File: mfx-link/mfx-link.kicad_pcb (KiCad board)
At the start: 2 copper layers, 50 x 50 mm, 59 parts, among them P1 CONN_01X02, P2 CONN_02X03, P3 CONN_01X02, P4 Grove I2C, P5 IBT-2, P6 CONN_01X02, P7 CONN_01X03, P8 Grove UART, P9 MFX, Q1 BC547, Q2 BC547, Q3 BC547, SW1 SW_PUSH, U1 LM393-1, U2 7805, U3 PIC16F1705, U4 6N137, U5 7805

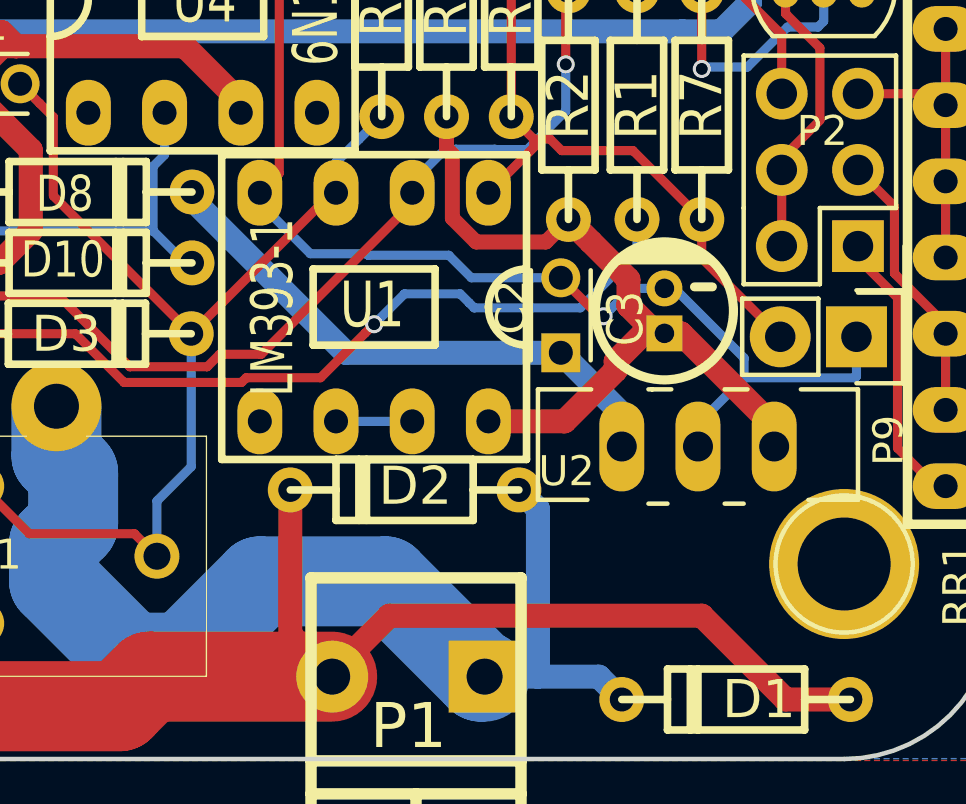
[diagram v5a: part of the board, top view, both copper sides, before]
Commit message: change caps
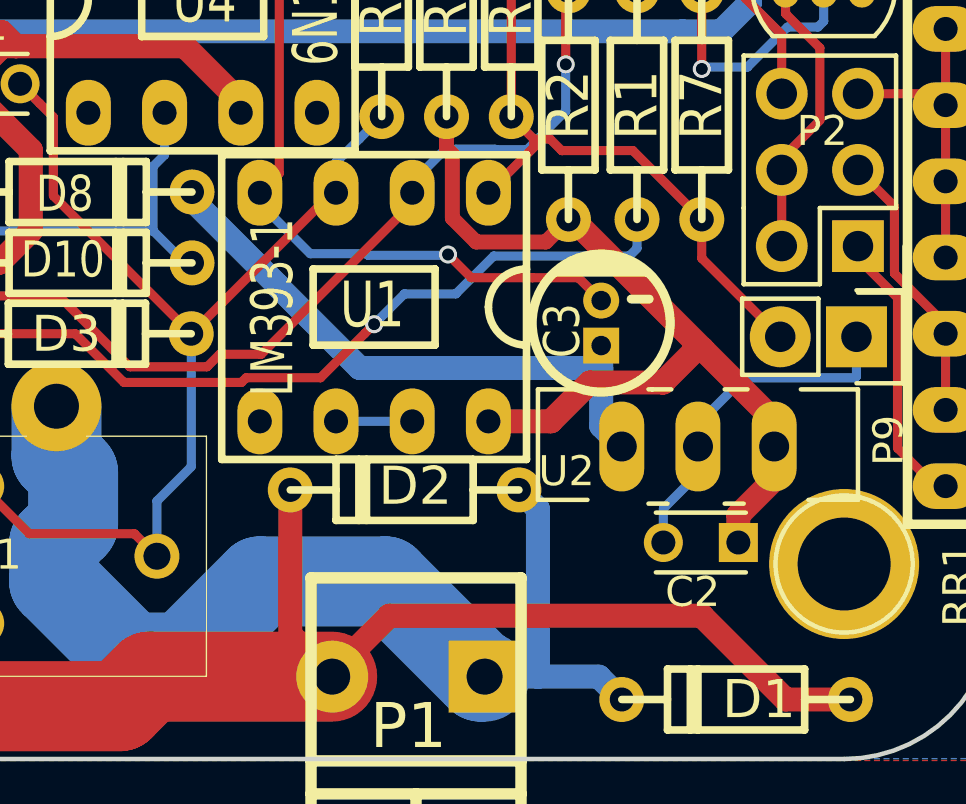
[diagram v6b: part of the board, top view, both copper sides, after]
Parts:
- Q1, Q2: value BC547 -> BC337
- moved C2 8.66 mm to (136.5, 122.8), turned to 180 degrees
- moved C3 2.15 mm to (131.9, 115.5)
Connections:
- C2 pad 1: /GVI -> VCC
- C3 pad 1: VCC -> /GVI
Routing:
- net VCC: track 26.1 -> 30.3 mm
- net GND: track 83.1 -> 79.9 mm
- net /GVI: track 18.8 -> 21.3 mm

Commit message: optimize placement
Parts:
- D8: value D -> 1N4007
- moved C2 3.90 mm to (132.6, 123.1), turned to 0 degrees
- moved C3 1.19 mm to (133.1, 115.4), turned to 90 degrees
- moved R14 0.38 mm to (112.1, 91.4)
- moved R12 0.25 mm to (109.9, 91.4)
- moved R10 0.13 mm to (107.6, 91.4)
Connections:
- C2 pad 1: VCC -> /GVI
- C3 pad 1: /GVI -> VCC
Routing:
- net GND: track 79.9 -> 102.9 mm, vias 8 -> 11
- net Net-(D11-Pad2): track 20.1 -> 16.8 mm, vias 2 -> 0
- net VCC: track 30.3 -> 27.6 mm
- net VDD: track 86.2 -> 87.7 mm
- net /GVI: track 21.3 -> 22.3 mm
- net Net-(P7-Pad2): track 23.8 -> 24.4 mm
- net /PULSE: track 48.4 -> 48.9 mm, vias 1 -> 2
- net GNDA: track 83.7 -> 83.5 mm, vias 6 -> 5

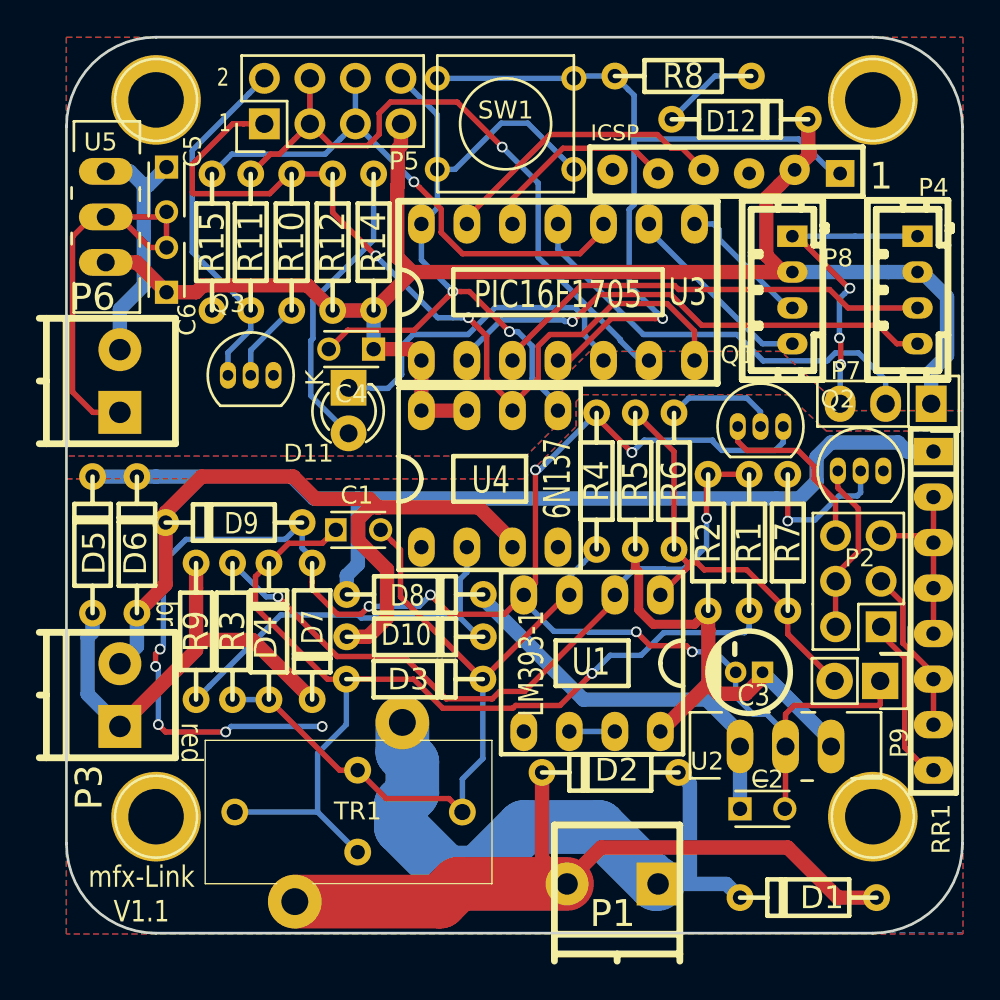
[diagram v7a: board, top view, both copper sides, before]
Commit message: fix BAT43 direction
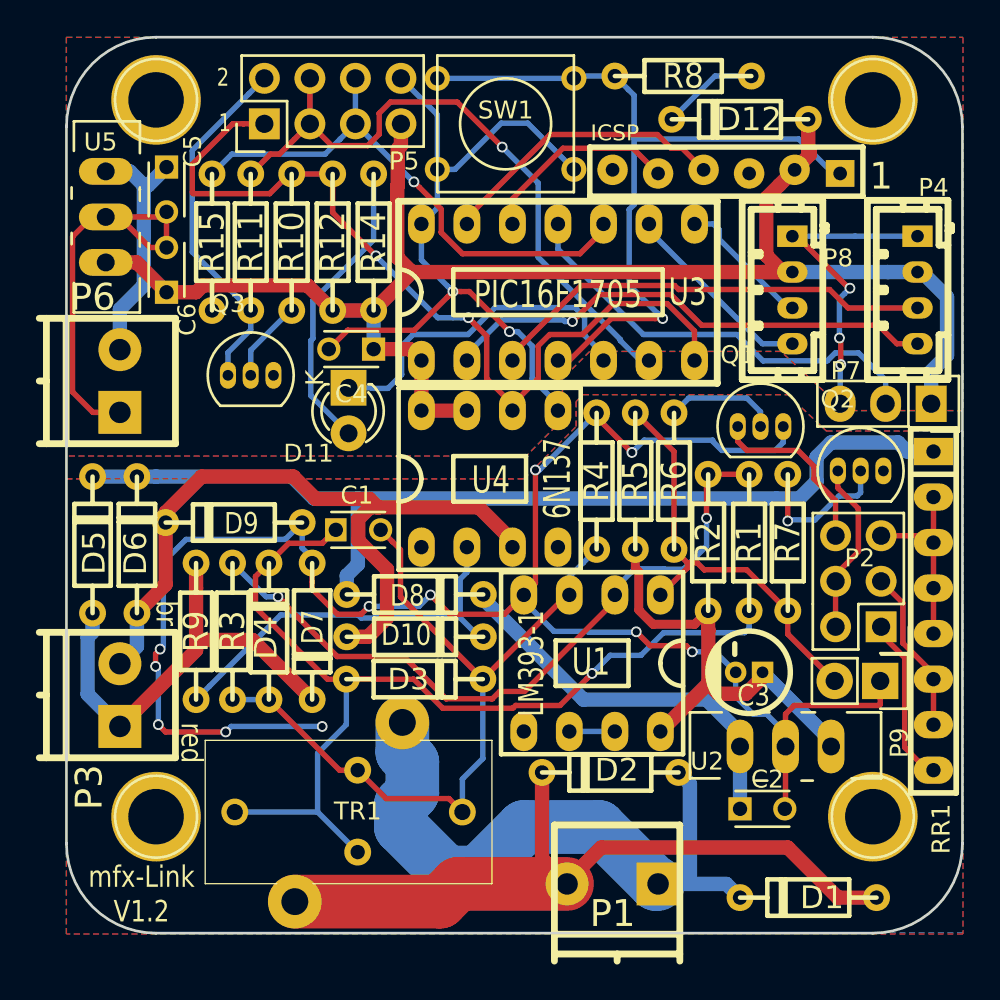
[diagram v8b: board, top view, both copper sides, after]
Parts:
- D1, D2, D5, D6, D7, D8, D9: value 1N4007 -> UF4007
- Q1, Q2: value BC337 -> BC517
- R11: value 1k -> 330
- turned D12 to 180 degrees
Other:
- board text added: "mfx-Link V1.2"
- board text removed: "mfx-Link V1.1"
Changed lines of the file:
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@@
     (links 122)
     (no_connects 0)
-    (area 91.9925 75.15 155 132.1752)
+    (area 94.924999 79.924999 145.075001 130.075001)
     (thickness 1.6)
     (drawings 16)
@@
       (effects (font (thickness 0.3048)))
     )
-    (fp_text value 1N4007 (at 0 -2.54 90) (layer F.SilkS) hide
+    (fp_text value UF4007 (at 0 -2.54 90) (layer F.SilkS) hide
       (effects (font (thickness 0.3048)))
     )
@@
       (effects (font (thickness 0.3048)))
     )
-    (fp_text value 1N4007 (at 0 -2.54 180) (layer F.SilkS) hide
+    (fp_text value UF4007 (at 0 -2.54 180) (layer F.SilkS) hide
       (effects (font (thickness 0.3048)))
     )
@@
       (effects (font (thickness 0.3048)))
     )
-    (fp_text value 1N4007 (at -5.0419 3.6322 180) (layer F.SilkS) hide
+    (fp_text value UF4007 (at -5.0419 3.6322 180) (layer F.SilkS) hide
       (effects (font (thickness 0.3048)))
     )
@@
       (effects (font (thickness 0.3048)))
     )
-    (fp_text value 1N4007 (at 0 -2.54 90) (layer F.SilkS) hide
+    (fp_text value UF4007 (at 0 -2.54 90) (layer F.SilkS) hide
       (effects (font (thickness 0.3048)))
     )
@@
       (effects (font (size 1.2 1) (thickness 0.25)))
     )
-    (fp_text value 1N4007 (at 0 -2.54 270) (layer F.SilkS) hide
+    (fp_text value UF4007 (at 0 -2.54 270) (layer F.SilkS) hide
       (effects (font (thickness 0.3048)))
     )
@@
       (effects (font (size 1.2 1) (thickness 0.25)))
     )
-    (fp_text value 1N4007 (at -0.2032 2.39268) (layer F.SilkS) hide
+    (fp_text value UF4007 (at -0.2032 2.39268) (layer F.SilkS) hide
       (effects (font (thickness 0.3048)))
     )
@@
       (effects (font (size 1.2 1) (thickness 0.25)))
     )
-    (fp_text value 1N4007 (at 0 -2.54 180) (layer F.SilkS) hide
+    (fp_text value UF4007 (at 0 -2.54 180) (layer F.SilkS) hide
       (effects (font (thickness 0.3048)))
     )
@@
       (effects (font (size 1.397 1.27) (thickness 0.2032)))
     )
-    (fp_text value 1k (at 0 2.032 270) (layer F.SilkS) hide
+    (fp_text value 330 (at 0 2.032 270) (layer F.SilkS) hide
       (effects (font (size 1.397 1.27) (thickness 0.2032)))
     )
@@
       (scale (xyz 1 1 1))
       (rotate (xyz 0 0 90))
-    )
-  )
-  (module w_pth_diodes:diode_do35 (layer F.Cu)
-    (at 132.588 84.582)
-    (descr "Diode, DO-35 package")
-    (fp_text reference D12 (at -0.508 0.127) (layer F.SilkS)
-      (effects (font (size 1.2 1) (thickness 0.25)))
-    )
-    (fp_text value BAT43 (at 16.7005 0.9525) (layer F.SilkS) hide
-      (effects (font (size 1.2 1) (thickness 0.25)))
-    )
-    (fp_line (start 1.524 1.016) (end 1.524 -1.016) (layer F.SilkS) (width 0.254))
-    (fp_line (start 1.27 -1.016) (end 1.27 1.016) (layer F.SilkS) (width 0.254))
-    (fp_line (start 3.81 0) (end 2.286 0) (layer F.SilkS) (width 0.254))
-    (fp_line (start -2.286 0) (end -3.81 0) (layer F.SilkS) (width 0.254))
-    (fp_line (start -2.286 -1.016) (end 2.286 -1.016) (layer F.SilkS) (width 0.254))
-    (fp_line (start 2.286 -1.016) (end 2.286 1.016) (layer F.SilkS) (width 0.254))
-    (fp_line (start 2.286 1.016) (end -2.286 1.016) (layer F.SilkS) (width 0.254))
-    (fp_line (start -2.286 1.016) (end -2.286 -1.016) (layer F.SilkS) (width 0.254))
-    (pad 1 thru_hole circle (at -3.81 0) (size 1.5 1.5) (drill 0.8) (layers *.Cu *.Mask F.SilkS)
-      (net 42 "Net-(D12-Pad1)"))
-    (pad 2 thru_hole circle (at 3.81 0) (size 1.5 1.5) (drill 0.8) (layers *.Cu *.Mask F.SilkS)
-      (net 13 VDD))
-    (model walter/pth_diodes/diode_do35.wrl
-      (at (xyz 0 0 0))
-      (scale (xyz 1 1 1))
-      (rotate (xyz 0 0 0))
     )
   )
@@
       (effects (font (size 1 1) (thickness 0.15)))
     )
-    (fp_text value BC337 (at 1.4605 -1.524) (layer F.Fab)
+    (fp_text value BC517 (at 1.4605 -1.524) (layer F.Fab)
       (effects (font (size 1 1) (thickness 0.15)))
     )
@@
       (effects (font (size 1 1) (thickness 0.15)))
     )
-    (fp_text value BC337 (at 1.2954 -1.4859) (layer F.Fab)
+    (fp_text value BC517 (at 1.2954 -1.4859) (layer F.Fab)
       (effects (font (size 1 1) (thickness 0.15)))
     )
@@
     )
   )
+  (module w_pth_diodes:diode_do35 (layer F.Cu)
+    (at 132.588 84.582 180)
+    (descr "Diode, DO-35 package")
+    (fp_text reference D12 (at -0.508 0 180) (layer F.SilkS)
+      (effects (font (size 1.3 1.3) (thickness 0.2)))
+    )
+    (fp_text value BAT43 (at 0 -2.54 180) (layer F.SilkS) hide
+      (effects (font (thickness 0.3048)))
+    )
+    (fp_line (start 1.524 1.016) (end 1.524 -1.016) (layer F.SilkS) (width 0.254))
+    (fp_line (start 1.27 -1.016) (end 1.27 1.016) (layer F.SilkS) (width 0.254))
+    (fp_line (start 3.81 0) (end 2.286 0) (layer F.SilkS) (width 0.254))
+    (fp_line (start -2.286 0) (end -3.81 0) (layer F.SilkS) (width 0.254))
+    (fp_line (start -2.286 -1.016) (end 2.286 -1.016) (layer F.SilkS) (width 0.254))
+    (fp_line (start 2.286 -1.016) (end 2.286 1.016) (layer F.SilkS) (width 0.254))
+    (fp_line (start 2.286 1.016) (end -2.286 1.016) (layer F.SilkS) (width 0.254))
+    (fp_line (start -2.286 1.016) (end -2.286 -1.016) (layer F.SilkS) (width 0.254))
+    (pad 1 thru_hole circle (at 3.81 0 180) (size 1.5 1.5) (drill 0.8) (layers *.Cu *.Mask F.SilkS)
+      (net 42 "Net-(D12-Pad1)"))
+    (pad 2 thru_hole circle (at -3.81 0 180) (size 1.5 1.5) (drill 0.8) (layers *.Cu *.Mask F.SilkS)
+      (net 13 VDD))
+    (model walter/pth_diodes/diode_do35.wrl
+      (at (xyz 0 0 0))
+      (scale (xyz 1 1 1))
+      (rotate (xyz 0 0 0))
+    )
+  )
   (dimension 50 (width 0.3) (layer Dwgs.User)
     (gr_text "50,000 mm" (at 148.35 105 90) (layer Dwgs.User)
@@
     (arrow2b (pts (xy 95 78) (xy 96.126504 77.413579)))
   )
-  (gr_text "mfx-Link\nV1.1" (at 99.187 127.8255) (layer F.SilkS)
+  (gr_text "mfx-Link\nV1.2" (at 99.187 127.8255) (layer F.SilkS)
     (effects (font (size 1.2 1) (thickness 0.2)))
   )
@@
   (via (at 130.7211 106.8451) (size 0.6) (drill 0.4) (layers F.Cu B.Cu) (net 11))
   (segment (start 125.6665 111.1885) (end 125.603 111.125) (width 0.3048) (layer B.Cu) (net 11))
+  (segment (start 137.668 119.5832) (end 137.668 120.6754) (width 0.8) (layer F.Cu) (net 12))
+  (segment (start 137.668 119.5832) (end 137.668 118.7196) (width 0.8) (layer F.Cu) (net 12))
   (segment (start 130.821002 113.085662) (end 130.81 113.07466) (width 0.8) (layer F.Cu) (net 12))
   (segment (start 130.821002 116.066998) (end 130.821002 113.085662) (width 0.8) (layer F.Cu) (net 12))
@@
   (segment (start 137.668 119.5832) (end 137.668 119.265) (width 0.8) (layer B.Cu) (net 12))
   (segment (start 137.668 119.265) (end 133.846 115.443) (width 0.8) (layer B.Cu) (net 12))
-  (segment (start 137.668 119.5832) (end 137.668 120.6754) (width 0.8) (layer F.Cu) (net 12))
-  (segment (start 137.668 119.5832) (end 137.668 118.7196) (width 0.8) (layer F.Cu) (net 12))
   (segment (start 130.9624 112.014) (end 130.81 112.014) (width 0.8) (layer F.Cu) (net 12))
   (segment (start 130.81 112.014) (end 130.060001 112.763999) (width 0.5) (layer F.Cu) (net 12))
@@
   (segment (start 114.173 97.409) (end 114.808 98.044) (width 0.8) (layer F.Cu) (net 13))
   (segment (start 136.398 86.3346) (end 136.398 84.582) (width 0.8) (layer F.Cu) (net 13))
+  (segment (start 97.1931 90.0303) (end 96.4431 90.0303) (width 0.3048) (layer F.Cu) (net 14))
+  (segment (start 96.4431 90.0303) (end 95.34069 91.13271) (width 0.3048) (layer F.Cu) (net 14))
+  (segment (start 95.34069 99.80049) (end 96.4772 100.937) (width 0.3048) (layer F.Cu) (net 14))
+  (segment (start 95.34069 91.13271) (end 95.34069 99.80049) (width 0.3048) (layer F.Cu) (net 14))
+  (segment (start 97.1931 90.0303) (end 100.3027 90.0303) (width 0.3048) (layer F.Cu) (net 14))
+  (segment (start 97.1931 90.0303) (end 97.9431 90.0303) (width 0.3048) (layer F.Cu) (net 14))
+  (segment (start 97.9431 90.0303) (end 99.6468 91.734) (width 0.3048) (layer F.Cu) (net 14))
+  (segment (start 99.6468 91.734) (end 99.664762 91.734) (width 0.3048) (layer F.Cu) (net 14))
   (segment (start 116.267728 94.495917) (end 116.567727 94.195918) (width 0.3048) (layer F.Cu) (net 14))
   (segment (start 114.808 90.424) (end 114.808 92.436191) (width 0.3048) (layer B.Cu) (net 14))
@@
   (segment (start 119.7229 96.4311) (end 117.487718 94.195918) (width 0.3048) (layer F.Cu) (net 14))
   (segment (start 110.697599 96.352401) (end 114.411244 96.352401) (width 0.3048) (layer F.Cu) (net 14))
-  (segment (start 97.1931 90.0303) (end 96.4431 90.0303) (width 0.3048) (layer F.Cu) (net 14))
-  (segment (start 96.4431 90.0303) (end 95.34069 91.13271) (width 0.3048) (layer F.Cu) (net 14))
-  (segment (start 95.34069 99.80049) (end 96.4772 100.937) (width 0.3048) (layer F.Cu) (net 14))
-  (segment (start 95.34069 91.13271) (end 95.34069 99.80049) (width 0.3048) (layer F.Cu) (net 14))
   (segment (start 96.4772 100.937) (end 97.982 100.937) (width 0.3048) (layer F.Cu) (net 14))
-  (segment (start 97.1931 90.0303) (end 100.3027 90.0303) (width 0.3048) (layer F.Cu) (net 14))
   (segment (start 100.3027 90.0303) (end 100.584 89.749) (width 0.3048) (layer F.Cu) (net 14))
   (segment (start 100.584 89.749) (end 100.584 91.734) (width 0.3048) (layer F.Cu) (net 14))
-  (segment (start 97.1931 90.0303) (end 97.9431 90.0303) (width 0.3048) (layer F.Cu) (net 14))
-  (segment (start 97.9431 90.0303) (end 99.6468 91.734) (width 0.3048) (layer F.Cu) (net 14))
-  (segment (start 99.6468 91.734) (end 99.664762 91.734) (width 0.3048) (layer F.Cu) (net 14))
   (segment (start 99.664762 91.734) (end 100.584 91.734) (width 0.3048) (layer F.Cu) (net 14))
   (segment (start 120.99098 99.05173) (end 120.99098 97.237881) (width 0.3048) (layer B.Cu) (net 14))
